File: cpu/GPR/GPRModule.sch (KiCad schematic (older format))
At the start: 51 parts, among them J1 Interconnect, U1 74HCT574, U10 74LS245, U11 74LS126, U2 74HCT574, U3 74LS245, U4 74LS245, U5 74LS245, U6 74LS245, U7 74LS245, U8 74LS245, U9 74LS245

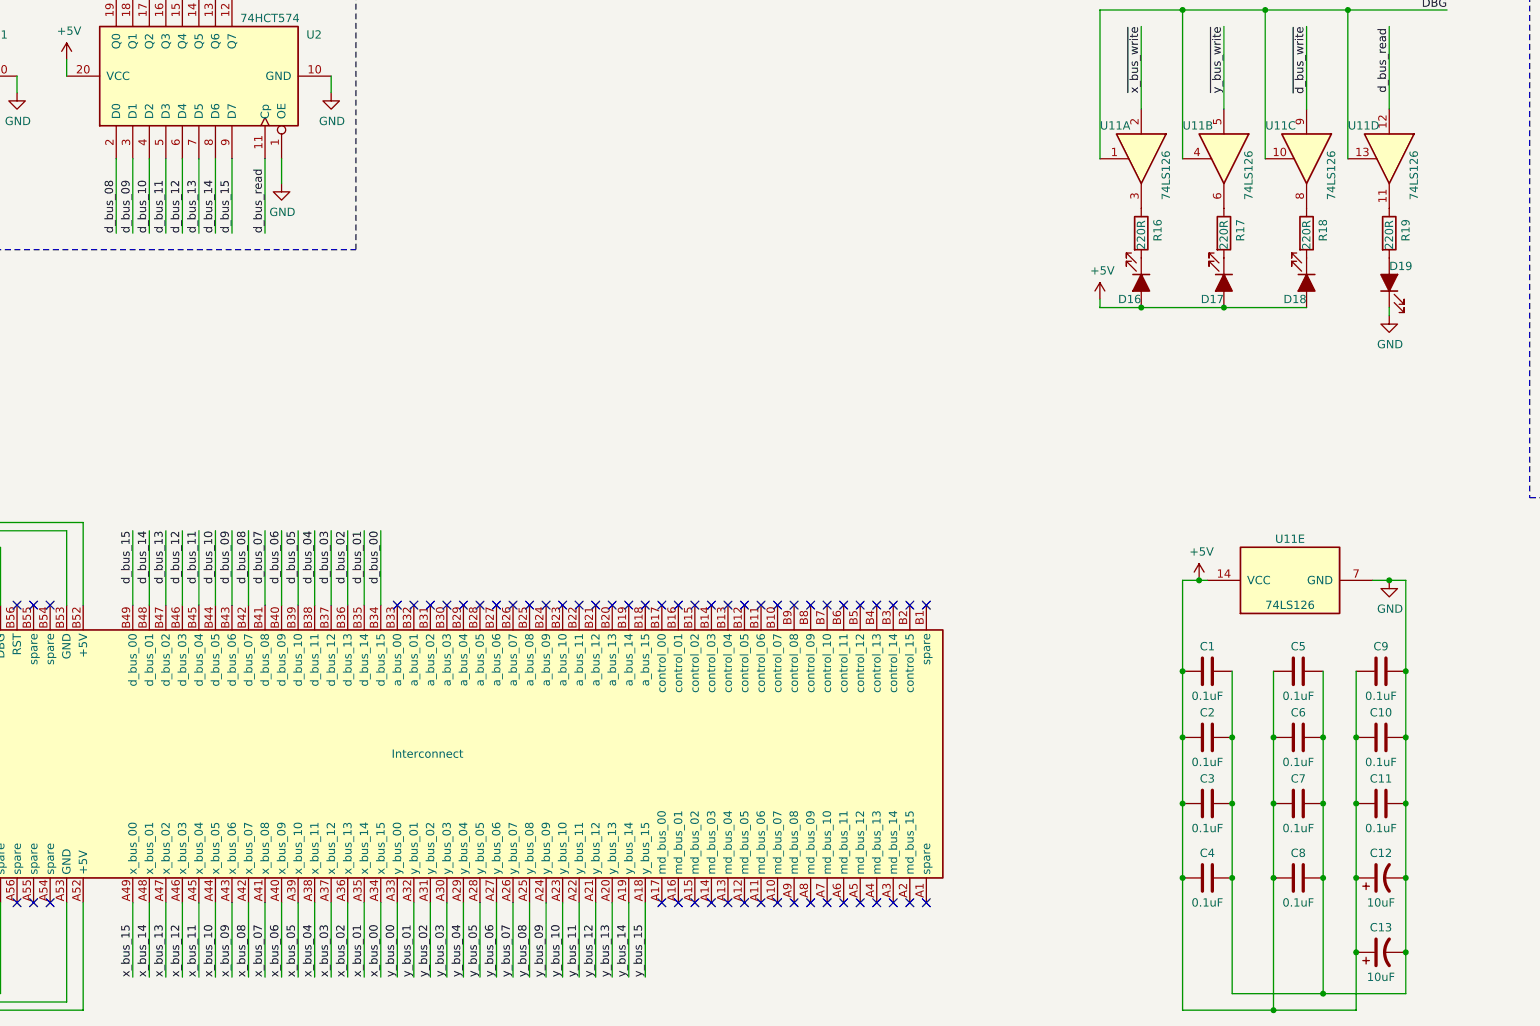
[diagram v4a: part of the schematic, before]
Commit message: Fixed errors on GPR after testing board. * writing too small * stat LEDs not aligned * stat buffer needed CE to be active low - swapped 126 for a 125 * x_bus was backwards on the interconnect
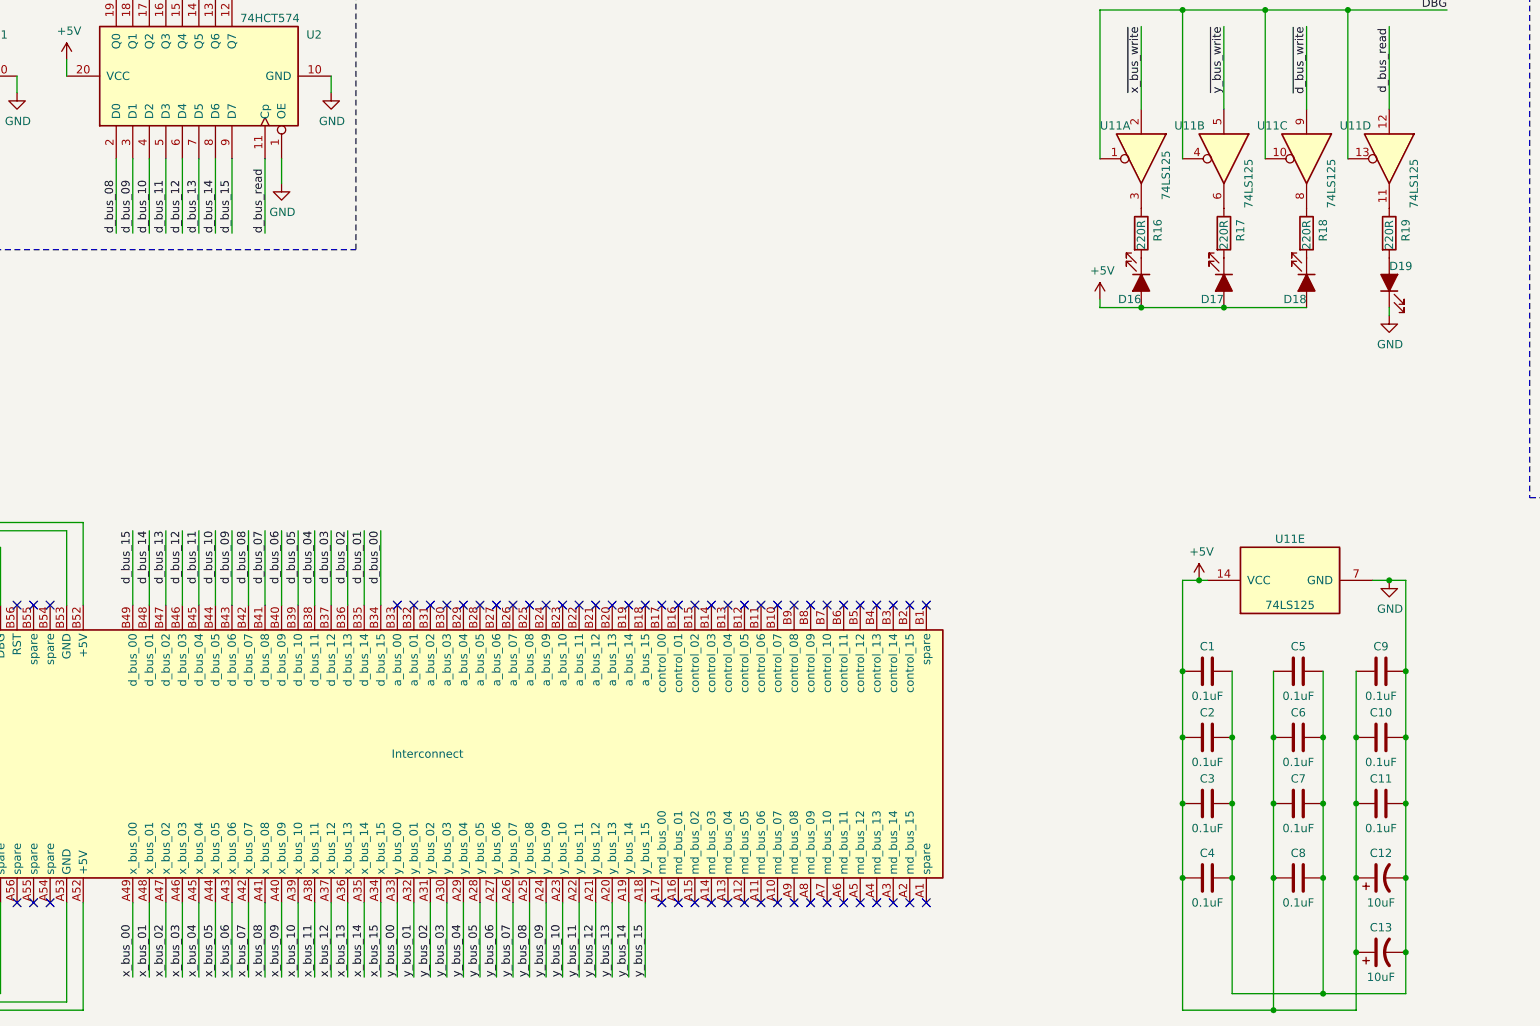
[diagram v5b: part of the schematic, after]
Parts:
- removed U11: 74LS126, Package_SO:SOIC-14_3.9x8.7mm_P1.27mm, symbol 74xx:74LS126
- added U11: 74LS125, Package_SO:SOIC-14_3.9x8.7mm_P1.27mm, symbol 74xx:74LS125
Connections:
- net +5V: now also U11.14 (VCC)
- net GND: now also U11.7 (GND)
- net d_bus_read: now also U11.12
- net x_bus_00: now also J1.A49 (x_bus_00); no longer J1.A34 (x_bus_15)
- net x_bus_01: now also J1.A48 (x_bus_01); no longer J1.A35 (x_bus_14)
- net x_bus_02: now also J1.A47 (x_bus_02); no longer J1.A36 (x_bus_13)
- net x_bus_03: now also J1.A46 (x_bus_03); no longer J1.A37 (x_bus_12)
- net x_bus_04: now also J1.A45 (x_bus_04); no longer J1.A38 (x_bus_11)
- net x_bus_05: now also J1.A44 (x_bus_05); no longer J1.A39 (x_bus_10)
- net x_bus_06: now also J1.A43 (x_bus_06); no longer J1.A40 (x_bus_09)
- net x_bus_07: now also J1.A42 (x_bus_07); no longer J1.A41 (x_bus_08)
- net x_bus_08: now also J1.A41 (x_bus_08); no longer J1.A42 (x_bus_07)
- net x_bus_09: now also J1.A40 (x_bus_09); no longer J1.A43 (x_bus_06)
- net x_bus_10: now also J1.A39 (x_bus_10); no longer J1.A44 (x_bus_05)
- net x_bus_11: now also J1.A38 (x_bus_11); no longer J1.A45 (x_bus_04)
- net x_bus_12: now also J1.A37 (x_bus_12); no longer J1.A46 (x_bus_03)
- net x_bus_13: now also J1.A36 (x_bus_13); no longer J1.A47 (x_bus_02)
- net x_bus_14: now also J1.A35 (x_bus_14); no longer J1.A48 (x_bus_01)
- net x_bus_15: now also J1.A34 (x_bus_15); no longer J1.A49 (x_bus_00)
- net ~DBG: now also U11.1, U11.10, U11.13, U11.4
- net ~d_bus_write: now also U11.9
- net ~x_bus_write: now also U11.2
- net ~y_bus_write: now also U11.5
- net at R16.1: now also U11.3
- net at R17.1: now also U11.6
- net at R18.1: now also U11.8
- net at R19.1: now also U11.11
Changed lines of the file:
@@
 Sheet 1 1
 Title "General Purpose Register"
-Date "2020-11-19"
-Rev "1.2"
+Date "2020-12-25"
+Rev "1.3"
 Comp ""
-Comment1 ""
+Comment1 "Does not use CLK signal for operation"
 Comment2 ""
 Comment3 ""
@@
 Wire Wire Line
 	6050 9450 6050 9900
-Text Label 4050 9900 1    50   ~ 0
-x_bus_12
-Text Label 3750 9900 1    50   ~ 0
-x_bus_15
-Wire Wire Line
-	4350 9450 4350 9900
-Text Label 4450 9900 1    50   ~ 0
-x_bus_08
-Wire Wire Line
-	4450 9450 4450 9900
-Text Label 4350 9900 1    50   ~ 0
-x_bus_09
-Text Label 4250 9900 1    50   ~ 0
-x_bus_10
-Wire Wire Line
-	4250 9450 4250 9900
-Text Label 4150 9900 1    50   ~ 0
-x_bus_11
-Wire Wire Line
-	4150 9450 4150 9900
-Wire Wire Line
-	3950 9450 3950 9900
-Wire Wire Line
-	4050 9450 4050 9900
-Text Label 3950 9900 1    50   ~ 0
-x_bus_13
-Text Label 3850 9900 1    50   ~ 0
-x_bus_14
-Wire Wire Line
-	3850 9450 3850 9900
-Wire Wire Line
-	3750 9450 3750 9900
-Text Label 4850 9900 1    50   ~ 0
-x_bus_04
-Text Label 4550 9900 1    50   ~ 0
-x_bus_07
-Wire Wire Line
-	5150 9450 5150 9900
-Text Label 5250 9900 1    50   ~ 0
-x_bus_00
-Wire Wire Line
-	5250 9450 5250 9900
-Text Label 5150 9900 1    50   ~ 0
-x_bus_01
-Text Label 5050 9900 1    50   ~ 0
-x_bus_02
-Wire Wire Line
-	5050 9450 5050 9900
-Text Label 4950 9900 1    50   ~ 0
-x_bus_03
-Wire Wire Line
-	4950 9450 4950 9900
-Wire Wire Line
-	4750 9450 4750 9900
-Wire Wire Line
-	4850 9450 4850 9900
-Text Label 4750 9900 1    50   ~ 0
-x_bus_05
-Text Label 4650 9900 1    50   ~ 0
-x_bus_06
-Wire Wire Line
-	4650 9450 4650 9900
-Wire Wire Line
-	4550 9450 4550 9900
 $Comp
 L power:+5V #PWR03
@@
 	1    11350 5400
 	1    0    0    -1
-$EndComp
-$Comp
-L 74xx:74LS126 U11
-U 1 1 5FA9CDD4
-P 9850 4950
-F 0 "U11" V 9650 4700 50  0000 L CNN
-F 1 "74LS126" H 9800 5100 50  0000 L CNN
-F 2 "Package_SO:SOIC-14_3.9x8.7mm_P1.27mm" H 9850 4950 50  0001 C CNN
-F 3 "http://www.ti.com/lit/gpn/sn74LS126" H 9850 4950 50  0001 C CNN
-F 4 "296-14546-1-ND" H 9850 4950 50  0001 C CNN "Digikey"
-	1    9850 4950
-	0    1    1    0
-$EndComp
-$Comp
-L 74xx:74LS126 U11
-U 2 1 5FA9DFAE
-P 10350 4950
-F 0 "U11" V 10150 4700 50  0000 L CNN
-F 1 "74LS126" H 10300 5100 50  0000 L CNN
-F 2 "Package_SO:SOIC-14_3.9x8.7mm_P1.27mm" H 10350 4950 50  0001 C CNN
-F 3 "http://www.ti.com/lit/gpn/sn74LS126" H 10350 4950 50  0001 C CNN
-F 4 "296-14546-1-ND" H 10350 4950 50  0001 C CNN "Digikey"
-	2    10350 4950
-	0    1    1    0
-$EndComp
-$Comp
-L 74xx:74LS126 U11
-U 3 1 5FAA00AC
-P 10850 4950
-F 0 "U11" V 10650 4700 50  0000 L CNN
-F 1 "74LS126" H 10800 5100 50  0000 L CNN
-F 2 "Package_SO:SOIC-14_3.9x8.7mm_P1.27mm" H 10850 4950 50  0001 C CNN
-F 3 "http://www.ti.com/lit/gpn/sn74LS126" H 10850 4950 50  0001 C CNN
-F 4 "296-14546-1-ND" H 10850 4950 50  0001 C CNN "Digikey"
-	3    10850 4950
-	0    1    1    0
-$EndComp
-$Comp
-L 74xx:74LS126 U11
-U 4 1 5FAA1BE0
-P 11350 4950
-F 0 "U11" V 11150 4700 50  0000 L CNN
-F 1 "74LS126" H 11300 5100 50  0000 L CNN
-F 2 "Package_SO:SOIC-14_3.9x8.7mm_P1.27mm" H 11350 4950 50  0001 C CNN
-F 3 "http://www.ti.com/lit/gpn/sn74LS126" H 11350 4950 50  0001 C CNN
-F 4 "296-14546-1-ND" H 11350 4950 50  0001 C CNN "Digikey"
-	4    11350 4950
-	0    1    1    0
 $EndComp
 Wire Wire Line
@@
 Connection ~ 10100 8050
 Connection ~ 11450 8050
-$Comp
-L 74xx:74LS126 U11
-U 5 1 614E36B3
-P 10750 7500
-F 0 "U11" V 11000 7500 50  0000 C CNN
-F 1 "74LS126" V 10600 7500 50  0000 C CNN
-F 2 "Package_SO:SOIC-14_3.9x8.7mm_P1.27mm" H 10750 7500 50  0001 C CNN
-F 3 "http://www.ti.com/lit/gpn/sn74LS126" H 10750 7500 50  0001 C CNN
-	5    10750 7500
-	0    -1   -1   0
-$EndComp
 Wire Wire Line
 	11450 7500 11350 7500
@@
 	2450 10100 2450 9450
 Connection ~ 2450 9450
+Wire Wire Line
+	4450 9450 4450 9900
+Wire Wire Line
+	4350 9450 4350 9900
+Text Label 4350 9900 1    50   ~ 0
+x_bus_06
+Text Label 4250 9900 1    50   ~ 0
+x_bus_05
+Wire Wire Line
+	4150 9450 4150 9900
+Wire Wire Line
+	4250 9450 4250 9900
+Wire Wire Line
+	4050 9450 4050 9900
+Text Label 4050 9900 1    50   ~ 0
+x_bus_03
+Wire Wire Line
+	3950 9450 3950 9900
+Text Label 3950 9900 1    50   ~ 0
+x_bus_02
+Text Label 3850 9900 1    50   ~ 0
+x_bus_01
+Wire Wire Line
+	3750 9450 3750 9900
+Text Label 3750 9900 1    50   ~ 0
+x_bus_00
+Wire Wire Line
+	3850 9450 3850 9900
+Text Label 4450 9900 1    50   ~ 0
+x_bus_07
+Text Label 4150 9900 1    50   ~ 0
+x_bus_04
+Wire Wire Line
+	5250 9450 5250 9900
+Wire Wire Line
+	5150 9450 5150 9900
+Text Label 5150 9900 1    50   ~ 0
+x_bus_14
+Text Label 5050 9900 1    50   ~ 0
+x_bus_13
+Wire Wire Line
+	4950 9450 4950 9900
+Wire Wire Line
+	5050 9450 5050 9900
+Wire Wire Line
+	4850 9450 4850 9900
+Text Label 4850 9900 1    50   ~ 0
+x_bus_11
+Wire Wire Line
+	4750 9450 4750 9900
+Text Label 4750 9900 1    50   ~ 0
+x_bus_10
+Text Label 4650 9900 1    50   ~ 0
+x_bus_09
+Wire Wire Line
+	4550 9450 4550 9900
+Text Label 4550 9900 1    50   ~ 0
+x_bus_08
+Wire Wire Line
+	4650 9450 4650 9900
+Text Label 5250 9900 1    50   ~ 0
+x_bus_15
+Text Label 4950 9900 1    50   ~ 0
+x_bus_12
+$Comp
+L 74xx:74LS125 U11
+U 1 1 5FF1FC65
+P 9850 4950
+F 0 "U11" V 9650 4700 50  0000 L CNN
+F 1 "74LS125" H 9800 5100 50  0000 L CNN
+F 2 "Package_SO:SOIC-14_3.9x8.7mm_P1.27mm" H 9850 4950 50  0001 C CNN
+F 3 "http://www.ti.com/lit/gpn/sn74LS125" H 9850 4950 50  0001 C CNN
+	1    9850 4950
+	0    1    1    0
+$EndComp
+$Comp
+L 74xx:74LS125 U11
+U 2 1 5FF22E69
+P 10350 4950
+F 0 "U11" V 10150 4650 50  0000 L CNN
+F 1 "74LS125" H 10350 5100 50  0000 L CNN
+F 2 "Package_SO:SOIC-14_3.9x8.7mm_P1.27mm" H 10350 4950 50  0001 C CNN
+F 3 "http://www.ti.com/lit/gpn/sn74LS125" H 10350 4950 50  0001 C CNN
+	2    10350 4950
+	0    1    1    0
+$EndComp
+$Comp
+L 74xx:74LS125 U11
+U 3 1 5FF24D72
+P 10850 4950
+F 0 "U11" V 10650 4650 50  0000 L CNN
+F 1 "74LS125" H 10850 5100 50  0000 L CNN
+F 2 "Package_SO:SOIC-14_3.9x8.7mm_P1.27mm" H 10850 4950 50  0001 C CNN
+F 3 "http://www.ti.com/lit/gpn/sn74LS125" H 10850 4950 50  0001 C CNN
+	3    10850 4950
+	0    1    1    0
+$EndComp
+$Comp
+L 74xx:74LS125 U11
+U 4 1 5FF2598E
+P 11350 4950
+F 0 "U11" V 11150 4650 50  0000 L CNN
+F 1 "74LS125" H 11350 5100 50  0000 L CNN
+F 2 "Package_SO:SOIC-14_3.9x8.7mm_P1.27mm" H 11350 4950 50  0001 C CNN
+F 3 "http://www.ti.com/lit/gpn/sn74LS125" H 11350 4950 50  0001 C CNN
+	4    11350 4950
+	0    1    1    0
+$EndComp
+$Comp
+L 74xx:74LS125 U11
+U 5 1 5FF2888E
+P 10750 7500
+F 0 "U11" V 11000 7500 50  0000 C CNN
+F 1 "74LS125" V 10600 7500 50  0000 C CNN
+F 2 "Package_SO:SOIC-14_3.9x8.7mm_P1.27mm" H 10750 7500 50  0001 C CNN
+F 3 "http://www.ti.com/lit/gpn/sn74LS125" H 10750 7500 50  0001 C CNN
+	5    10750 7500
+	0    -1   -1   0
+$EndComp
 $EndSCHEMATC
